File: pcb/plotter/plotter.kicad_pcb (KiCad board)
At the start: 2 copper layers, 216.4 x 34.3 mm, 61 parts, among them J1 SH 1106 Display, J10 Limit switches, J11 GRBL switches???, J2 SWD, J3 Console, J4 Micro_SD_Card_Det, J5 USB_B_Micro, J6 Barrel_Jack_Switch, J7 Servo, J8 Motor2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

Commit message: Moving to STM32F405 and the final pinout (as on the PCB in the future).
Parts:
- moved J7 3.70 mm to (112.3, 124.0)
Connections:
- J4 pad 10: unconnected-(J4-Pad10) -> /sdCardDetA
- J4 pad 11: unconnected-(J4-Pad11) -> GND
- J4 pad 4: unconnected-(J4-Pad4) -> VDD
- J4 pad 6: unconnected-(J4-Pad6) -> GND
- J4 pad 9: unconnected-(J4-Pad9) -> /sdCardDetB
- U1 pad 30: /servo -> unconnected-(U1-Pad30)
- U1 pad 33: unconnected-(U1-Pad33) -> /sdCardDetA
- U1 pad 34: unconnected-(U1-Pad34) -> /sdCardDetB
- U1 pad 61: unconnected-(U1-Pad61) -> /servo

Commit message: PCB and 3d model. Still work in progress.
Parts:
- removed J11: GRBL switches???, Connector_PinHeader_2.54mm:PinHeader_1x04_P2.54mm_Vertical
- removed J7: Servo, Connector_PinHeader_2.54mm:PinHeader_1x03_P2.54mm_Vertical
- added C38: 100nF, Capacitor_SMD:C_0603_1608Metric, F.Cu at (258.1, 92.5)
- added C39: 100nF, Capacitor_SMD:C_0603_1608Metric, F.Cu at (234.8, 96.0)
- added C40: 100nF, Capacitor_SMD:C_0603_1608Metric, F.Cu at (230.6, 106.2)
- added C41: 100nF, Capacitor_SMD:C_0603_1608Metric, F.Cu at (230.6, 112.3)
- added C42: 100nF, Capacitor_SMD:C_0603_1608Metric, F.Cu at (129.4, 97.9)
- added C43: 100nF, Capacitor_SMD:C_0603_1608Metric, F.Cu at (129.4, 100.0)
- added C44: 100nF, Capacitor_SMD:C_0603_1608Metric, F.Cu at (129.4, 102.0)
- added C45: 100nF, Capacitor_SMD:C_0603_1608Metric, F.Cu at (129.4, 104.0)
- added R10: 1k, Resistor_SMD:R_0603_1608Metric, F.Cu at (125.9, 102.0)
- added R11: 1k, Resistor_SMD:R_0603_1608Metric, F.Cu at (125.9, 104.0)
- added R5: 1k, Resistor_SMD:R_0603_1608Metric, F.Cu at (234.7, 93.5)
- added R6: 1k, Resistor_SMD:R_0603_1608Metric, F.Cu at (230.6, 108.2)
- added R7: 1k, Resistor_SMD:R_0603_1608Metric, F.Cu at (230.6, 110.2)
- added R8: 1k, Resistor_SMD:R_0603_1608Metric, F.Cu at (125.9, 97.9)
- added R9: 1k, Resistor_SMD:R_0603_1608Metric, F.Cu at (125.9, 100.0)
- added U6: AP1117-33, Package_TO_SOT_SMD:SOT-223-3_TabPin2, F.Cu at (216.9, 113.8)
- added U7: PUSB3F96, Package_DFN_QFN:Diodes_UDFN-10_1.0x2.5mm_P0.5mm, F.Cu at (251.0, 91.4)
- added U8: PUSB3F96, Package_DFN_QFN:Diodes_UDFN-10_1.0x2.5mm_P0.5mm, F.Cu at (225.0, 93.5)
- C1, C29, C35, C37: footprint Capacitor_THT:CP_Radial_D13.0mm_P5.00mm -> Capacitor_SMD:CP_Elec_8x10
- F1: value Fuse -> Polyfuse; footprint Fuse:Fuseholder_Cylinder-5x20mm_Bulgin_FX0456_Vertical_Closed -> Fuse:Fuse_1812_4532Metric
- J1: footprint Connector_PinHeader_2.54mm:PinHeader_1x04_P2.54mm_Vertical -> iwasz:SH1106
- J10: footprint Connector_PinHeader_2.54mm:PinHeader_1x05_P2.54mm_Vertical -> Connector_JST:JST_PH_B8B-PH-K_1x08_P2.00mm_Vertical
- J4: footprint Connector_Card:microSD_HC_Hirose_DM3AT-SF-PEJM5 -> iwasz:microSD_HC_Hirose_DM3AT-SF-PEJM5
- J5: footprint Connector_USB:USB_Micro-B_Amphenol_10104110_Horizontal -> iwasz:USB_Micro-B_Amphenol_10104110_Horizontal
- J6: footprint Connector_BarrelJack:BarrelJack_Horizontal -> iwasz:BarrelJack_Horizontal
- J8, J9: footprint Connector_PinHeader_2.54mm:PinHeader_1x04_P2.54mm_Vertical -> Connector_JST:JST_PH_B4B-PH-K_1x04_P2.00mm_Vertical
- SW1: footprint Rotary_Encoder:RotaryEncoder_Alps_EC11E-Switch_Vertical_H20mm -> iwasz:RotaryEncoder_Alps_EC11E_Vertical_H20mm
- SW2: footprint Button_Switch_THT:SW_CuK_OS102011MA1QN1_SPDT_Angled -> iwasz:MFP 201 NR_copy
- U2, U3: footprint Module:Pololu_Breakout-16_15.2x20.3mm -> iwasz:Pololu_Breakout-16_15.2x20.3mm
- U4: value MIC5504-3.3YM5 -> PUSB3F96; footprint Package_TO_SOT_SMD:SOT-23-5 -> Package_DFN_QFN:Diodes_UDFN-10_1.0x2.5mm_P0.5mm
- moved C30 76.8 mm to (112.8, 92.5)
- moved C27 74.5 mm to (98.0, 93.0)
- moved C34 73.1 mm to (98.0, 107.2)
- moved C26 70.5 mm to (98.0, 90.4)
- moved C33 69.1 mm to (98.0, 109.7)
- moved C28 65.7 mm to (98.0, 95.5)
- moved C3 58.4 mm to (112.8, 108.7)
- moved C31 58.1 mm to (112.8, 90.4)
- moved C37 56.7 mm to (83.8, 110.7), turned to 180 degrees
- moved C32 48.9 mm to (98.0, 112.8)
- moved U4 42.0 mm to (245.9, 112.8), turned to 180 degrees
- moved FB1 36.1 mm to (72.9, 108.7)
- moved C1 35.3 mm to (83.8, 101.6), turned to 180 degrees
- moved J6 30.7 mm to (90.4, 95.0), turned to -90 degrees
- moved C2 28.2 mm to (112.8, 106.7)
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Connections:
- C2 pad 2: VDD -> +5V
- C3 pad 2: VDD -> +5V
- C30 pad 2: VDD -> +5V
- C31 pad 2: VDD -> +5V
- C36 pad 1: unconnected-(C36-Pad1) -> GND
- C36 pad 2: unconnected-(C36-Pad2) -> VDD
- J10 pad 1: /limitL -> Net-(J10-Pad1)
- J10 pad 2: /limitR -> Net-(J10-Pad2)
- J10 pad 3: /limitT -> Net-(J10-Pad3)
- J10 pad 4: /limitB -> Net-(J10-Pad4)
- J4 pad 10: /sdCardDetA -> /esd1
- J4 pad 3: unconnected-(J4-Pad3) -> Net-(J4-Pad3)
- J4 pad 8: Net-(J4-Pad8) -> unconnected-(J4-Pad8)
- J4 pad 9: /sdCardDetB -> /esd2
- J5 pad 6: unconnected-(J5-Pad6) -> GND
- SW1 pad A: Net-(SW1-PadA) -> /esd3
- SW1 pad B: Net-(SW1-PadB) -> /esd4
- SW1 pad C: unconnected-(SW1-PadC) -> GND
- SW1 pad S1: /switchEnter -> Net-(R5-Pad2)
- U1 pad 23: Net-(J4-Pad8) -> Net-(J4-Pad3)
- U1 pad 24: Net-(SW1-PadA) -> Net-(C40-Pad1)
- U1 pad 25: Net-(SW1-PadB) -> Net-(C41-Pad1)
- U1 pad 27: /limitT -> unconnected-(U1-Pad27)
- U1 pad 33: /sdCardDetA -> /limitT
- U1 pad 34: /sdCardDetB -> /esd1
- U1 pad 35: unconnected-(U1-Pad35) -> /esd2
- U2 pad 2: VDD -> +5V
- U3 pad 2: VDD -> +5V
- U4 pad 1: +5V -> /switchEnter
- U4 pad 2: GND -> /esd3
- U4 pad 3: +5V -> GND
- U4 pad 4: unconnected-(U4-Pad4) -> /esd4
- U4 pad 5: VDD -> unconnected-(U4-Pad5)
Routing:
- net /sckMotor: track 0.00 -> 133.5 mm, vias 0 -> 2
- net /Motors/mosiMotor: track 0.00 -> 132.9 mm, vias 0 -> 4
- net /enable2: track 0.00 -> 129.4 mm, vias 0 -> 2
- net +5V: track 0.00 -> 127.4 mm, vias 0 -> 1
- net /Motors/nssMotor2: track 0.00 -> 126.9 mm, vias 0 -> 4
- net /servo: track 0.00 -> 126.5 mm, vias 0 -> 2
- net /Motors/nssMotor1: track 0.00 -> 124.8 mm, vias 0 -> 2
- net /Motors/misoMotor: track 0.00 -> 123.0 mm, vias 0 -> 3
- net /enable1: track 0.00 -> 121.5 mm, vias 0 -> 2
- net /limitL: track 0.00 -> 118.4 mm, vias 0 -> 2
- net /step2: track 0.00 -> 113.1 mm, vias 0 -> 1
- net /dir2: track 0.00 -> 108.9 mm, vias 0 -> 1
- net /step1: track 0.00 -> 104.9 mm, vias 0 -> 2
- net /dir1: track 0.00 -> 104.5 mm, vias 0 -> 2
- net /limitR: track 0.00 -> 104.5 mm, vias 0 -> 2
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- added copper zone on B.Cu, net GND
- added copper zone on F.Cu, net GND
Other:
- board text added: "Motor1"
- board text added: "Motor2"

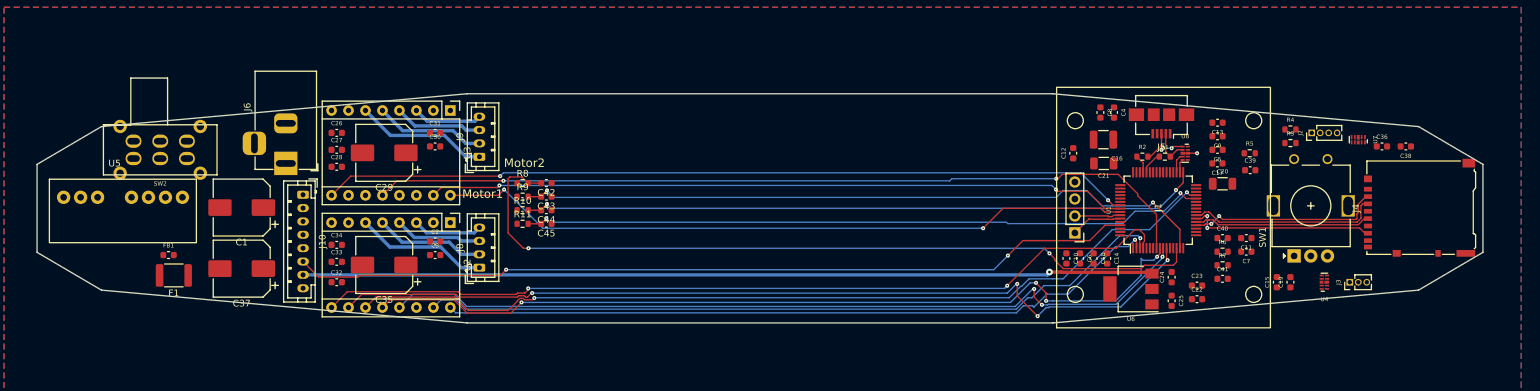
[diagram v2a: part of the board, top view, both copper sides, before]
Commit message: Thread priorites.
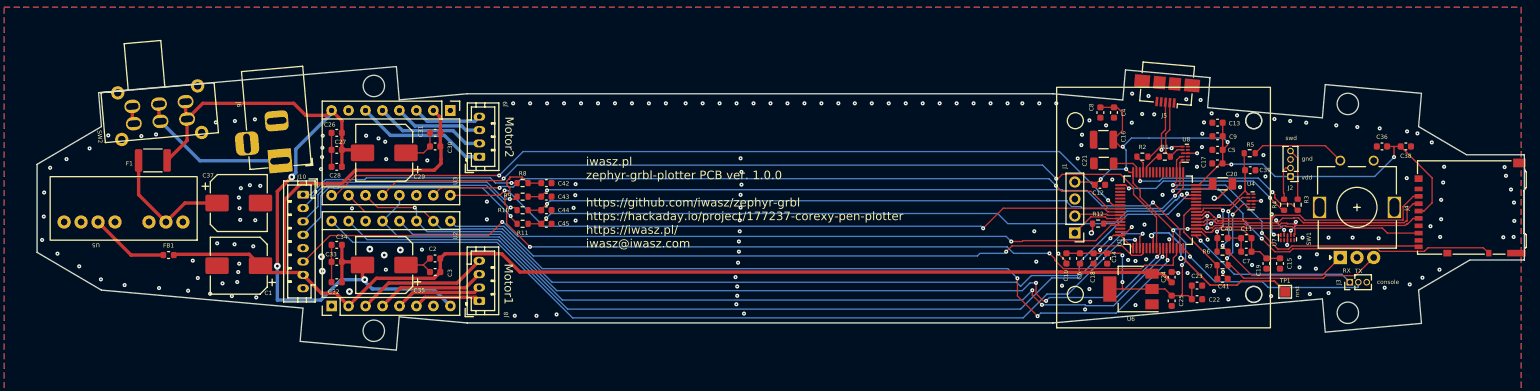
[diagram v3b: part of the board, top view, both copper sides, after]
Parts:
- added R12: 22R, Resistor_SMD:R_0603_1608Metric, F.Cu at (212.0, 104.0)
- added TP1: Reset, TestPoint:TestPoint_Pad_1.5x1.5mm, F.Cu at (240.0, 114.2)
- U4, U7, U8: footprint Package_DFN_QFN:Diodes_UDFN-10_1.0x2.5mm_P0.5mm -> iwasz:Diodes_UDFN-10_1.0x2.5mm_P0.5mm
- moved U2 21.7 mm to (97.3, 116.3), turned to 90 degrees
- moved U7 18.1 mm to (240.3, 106.1)
- moved F1 17.5 mm to (70.5, 94.5)
- moved U4 16.4 mm to (234.9, 100.6), turned to 0 degrees
- moved R4 11.3 mm to (239.8, 101.2), turned to 90 degrees
- moved C37 9.83 mm to (83.4, 100.9), turned to 0 degrees
- moved R3 9.30 mm to (241.9, 101.2), turned to 90 degrees
- moved C1 8.71 mm to (83.4, 110.3)
- moved J4 7.58 mm to (267.7, 101.6)
- moved J2 7.26 mm to (240.8, 97.0), turned to 180 degrees
- moved SW1 6.91 mm to (248.2, 109.1)
- moved C12 6.19 mm to (212.3, 98.2), turned to 0 degrees
- moved SW2 5.56 mm to (71.5, 87.4), turned to 5 degrees
- moved J8 4.97 mm to (119.4, 115.6)
- moved J5 4.76 mm to (222.2, 84.3), turned to 175 degrees
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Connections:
- C2 pad 1: Net-(C2-Pad1) -> GND
- C26 pad 1: Net-(C26-Pad1) -> GND
- C27 pad 1: Net-(C26-Pad1) -> GND
- C28 pad 1: Net-(C26-Pad1) -> GND
- C29 pad 1: Net-(C26-Pad1) -> GND
- C3 pad 1: Net-(C2-Pad1) -> GND
- C30 pad 1: Net-(C30-Pad1) -> GND
- C31 pad 1: Net-(C30-Pad1) -> GND
- C32 pad 1: Net-(C32-Pad1) -> GND
- C33 pad 1: Net-(C32-Pad1) -> GND
- C34 pad 1: Net-(C32-Pad1) -> GND
- C35 pad 1: Net-(C32-Pad1) -> GND
- U1 pad 60: unconnected-(U1-Pad60) -> Net-(U1-Pad60)
- U1 pad 7: unconnected-(U1-Pad7) -> Net-(U1-Pad7)
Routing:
- net VDD: track 0.00 -> 177.6 mm, vias 0 -> 13
- net +24V: track 0.00 -> 117.9 mm, vias 0 -> 3
- net +5V: track 127.4 -> 203.8 mm, vias 1 -> 0
- net /esd1: track 2.02 -> 58.0 mm, vias 0 -> 2
- net GND: track 2.13 -> 46.8 mm, vias 1 -> 201
- net /esd2: track 2.93 -> 47.1 mm, vias 0 -> 2
- net Net-(J10-Pad4): track 0.00 -> 39.2 mm, vias 0 -> 1
- net Net-(J10-Pad3): track 0.00 -> 36.9 mm, vias 0 -> 1
- net Net-(J10-Pad2): track 0.00 -> 35.0 mm, vias 0 -> 1
- net /esd4: track 0.00 -> 34.9 mm, vias 0 -> 2
- net Net-(J10-Pad1): track 0.00 -> 33.4 mm, vias 0 -> 1
- net /esd3: track 0.00 -> 30.0 mm, vias 0 -> 2
- net Net-(J3-Pad2): track 0.00 -> 29.5 mm, vias 0 -> 1
- net Net-(U1-Pad7): track 0.00 -> 27.5 mm, vias 0 -> 2
- net Net-(R3-Pad1): track 0.00 -> 27.4 mm, vias 0 -> 2
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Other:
- board size 216.4 x 34.3 mm -> 222.6 x 42.4 mm
- board text added: "RX"
- board text added: "TX"
- board text added: "console"
- board text added: "gnd"
- board text added: "iwasz.pl zephyr-grbl-plotter PCB ver. 1.0.0 https://github.com/iwasz/zephyr-grbl https://hackaday.io/project/177237-corexy-pen-plotter https://iwasz.pl/ iwasz@iwasz.com"
- board text added: "nrst"
- board text added: "swd"
- board text added: "vdd"

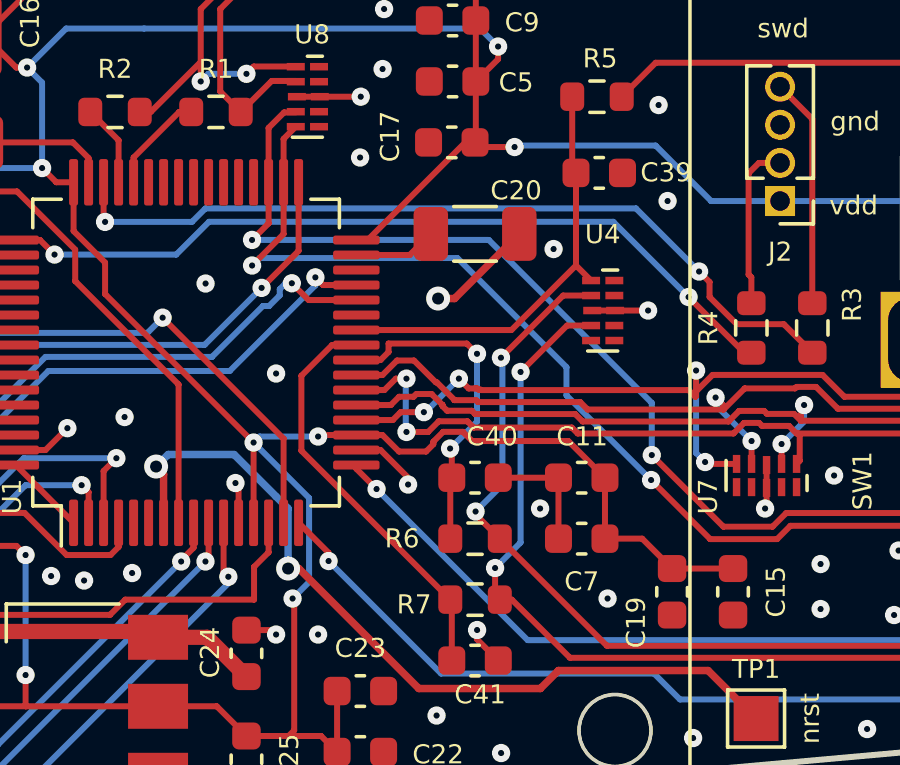
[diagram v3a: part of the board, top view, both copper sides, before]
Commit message: Communication with the GRBL for SD card impl.
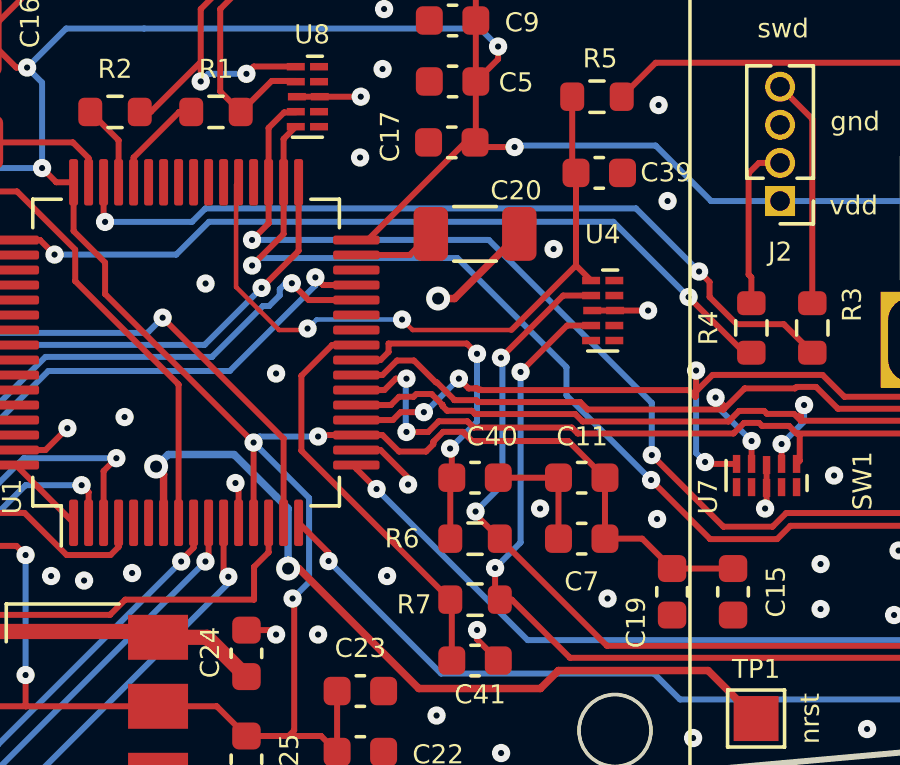
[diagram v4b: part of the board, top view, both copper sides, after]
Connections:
- U1 pad 26: /switchEnter -> unconnected-(U1-Pad26)
- U1 pad 37: unconnected-(U1-Pad37) -> /switchEnter
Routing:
- net /switchEnter: track 14.6 -> 23.0 mm, vias 0 -> 2
- net GND: vias 201 -> 203

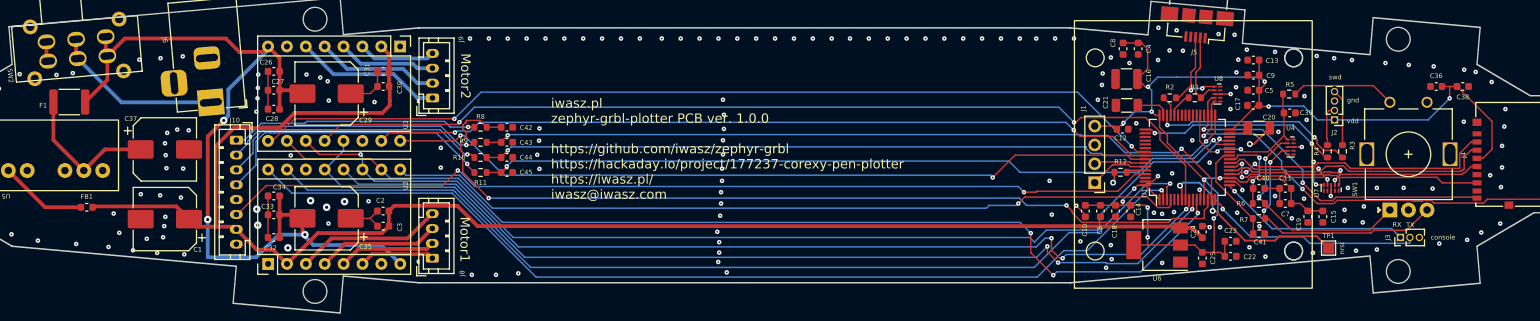
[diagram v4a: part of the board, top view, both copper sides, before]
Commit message: I finally got the SD card to work.
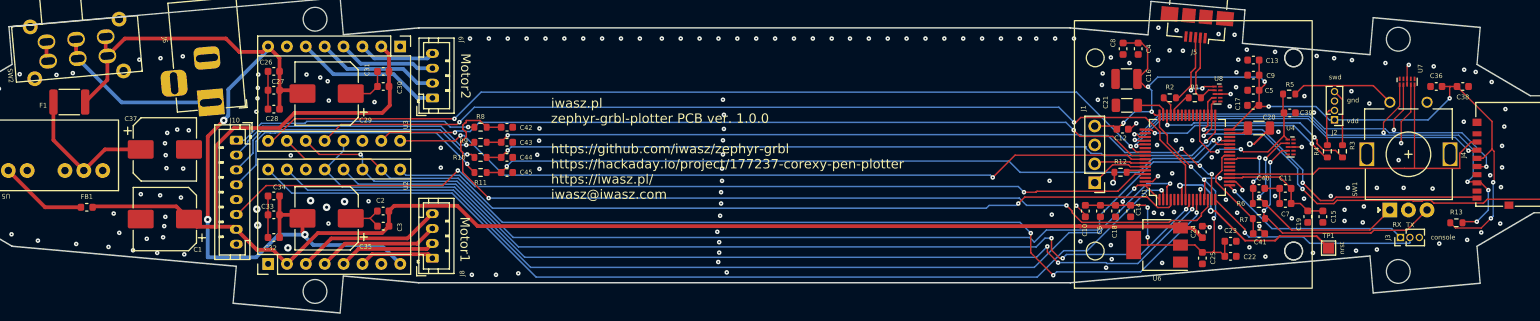
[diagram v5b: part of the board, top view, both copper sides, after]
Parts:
- added R13: 10k, Resistor_SMD:R_0603_1608Metric, F.Cu at (257.2, 110.8)
- moved U7 17.6 mm to (250.6, 91.8), turned to 90 degrees
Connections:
- J4 pad 3: Net-(J4-Pad3) -> /sdMosi
- J4 pad 5: Net-(J4-Pad5) -> /sdSck
- J4 pad 7: Net-(J4-Pad7) -> /sdMiso
- U1 pad 21: Net-(J4-Pad5) -> unconnected-(U1-Pad21)
- U1 pad 22: Net-(J4-Pad7) -> unconnected-(U1-Pad22)
- U1 pad 23: Net-(J4-Pad3) -> unconnected-(U1-Pad23)
- U1 pad 51: unconnected-(U1-Pad51) -> /sdSck
- U1 pad 52: unconnected-(U1-Pad52) -> /sdMiso
- U1 pad 53: unconnected-(U1-Pad53) -> /sdMosi
- U7 pad 1: Net-(J4-Pad7) -> /sdMiso
- U7 pad 2: Net-(J4-Pad5) -> /sdSck
- U7 pad 4: Net-(J4-Pad3) -> /sdMosi
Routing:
- net /sdMiso: track 0.00 -> 72.3 mm, vias 0 -> 5
- net /sdSck: track 0.00 -> 62.0 mm, vias 0 -> 3
- net /sdMosi: track 0.00 -> 59.8 mm, vias 0 -> 3
- net Net-(J4-Pad3): track 40.2 -> 0.00 mm, vias 2 -> 0
- net Net-(J4-Pad5): track 37.4 -> 0.00 mm, vias 2 -> 0
- net Net-(J4-Pad7): track 37.3 -> 0.00 mm, vias 2 -> 0
- net VDD: track 177.6 -> 191.8 mm, vias 13 -> 16
- net Net-(J4-Pad2): track 42.6 -> 47.5 mm, vias 4 -> 0
- net GND: track 46.8 -> 49.2 mm, vias 203 -> 209
- net +24V: track 117.9 -> 115.8 mm
- net /esd1: track 58.0 -> 58.7 mm
- net /enable1: track 124.1 -> 123.5 mm
- net +5V: track 203.8 -> 203.2 mm
- net Net-(C40-Pad1): track 11.1 -> 10.6 mm
- net /limitR: track 103.7 -> 104.1 mm, vias 2 -> 4
